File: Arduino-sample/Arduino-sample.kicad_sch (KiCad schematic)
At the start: 7 parts, among them U1 NJM78L05SU3

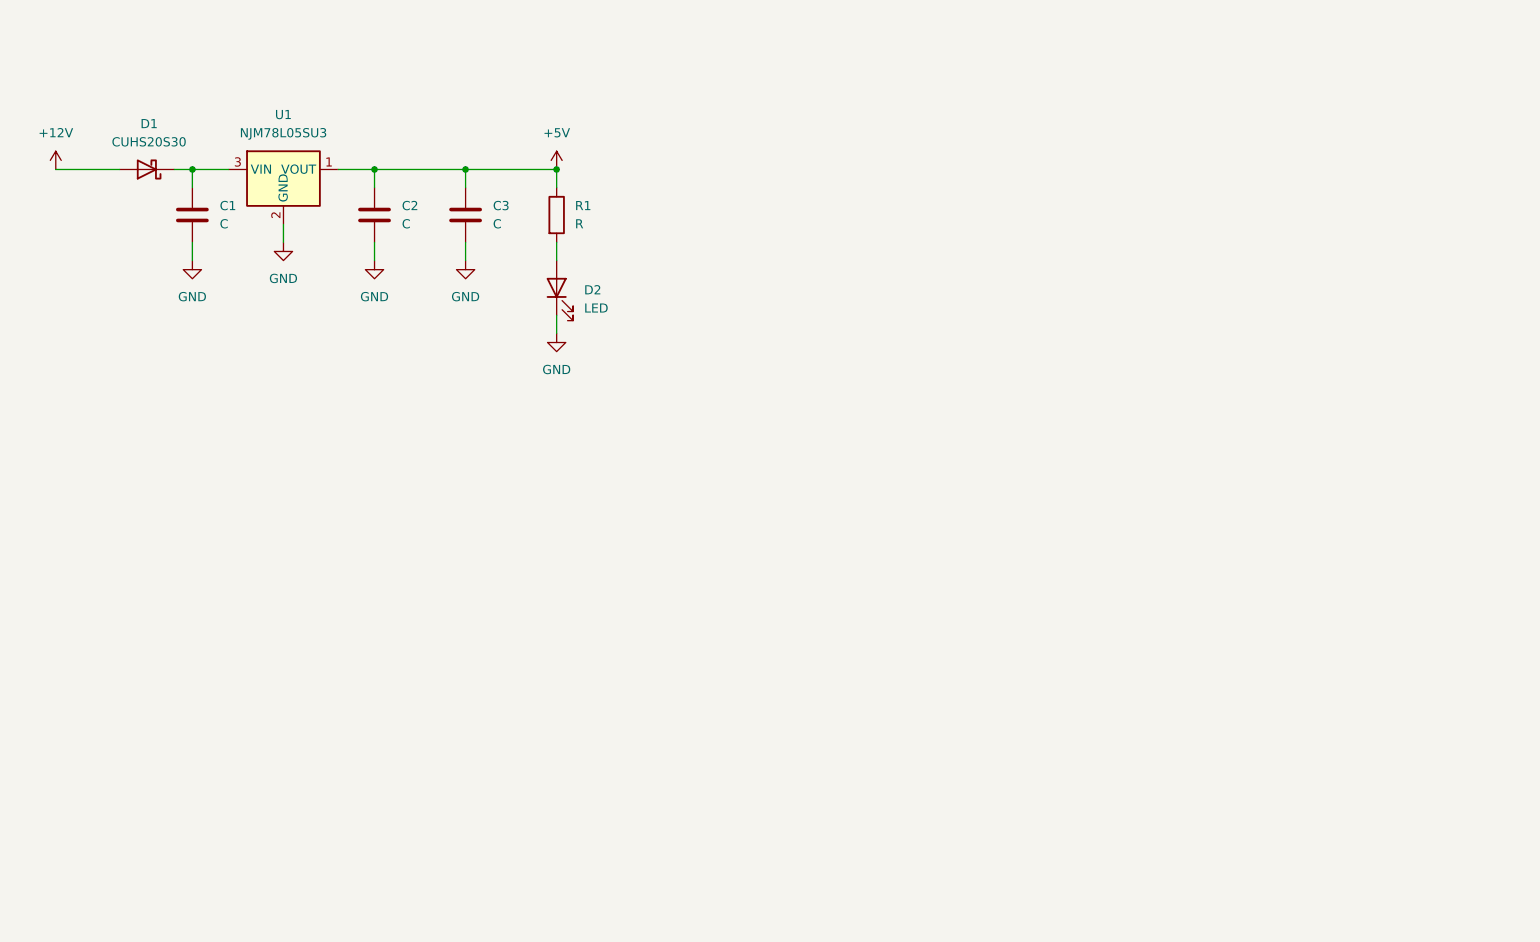
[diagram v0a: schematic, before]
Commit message: マイコン周辺回路追加
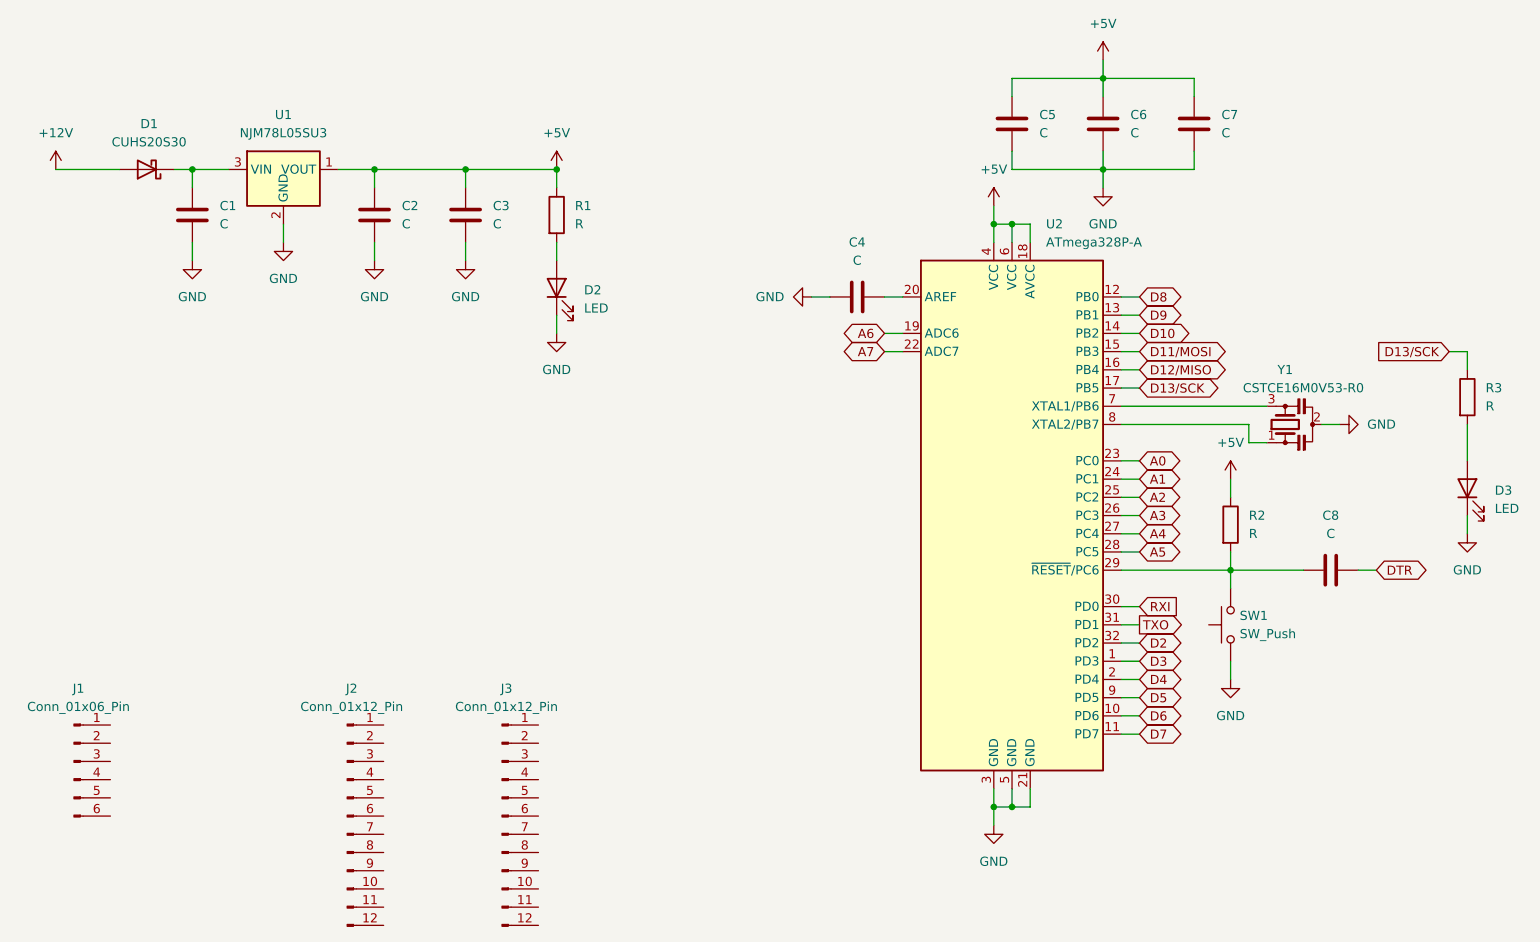
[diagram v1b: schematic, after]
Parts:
- added C4, C5, C6, C7, C8: C, symbol Device:C
- added D3: LED, symbol Device:LED
- added J1: Conn_01x06_Pin, symbol Connector:Conn_01x06_Pin
- added J2, J3: Conn_01x12_Pin, symbol Connector:Conn_01x12_Pin
- added R2, R3: R, symbol Device:R
- added SW1: SW_Push, symbol Switch:SW_Push
- added U2: ATmega328P-A, ProjectEV:TQFP-32_7x7mm_P0.8mm, symbol ProjectEV:ATmega328P-A
- added Y1: CSTCE16M0V53-R0, ProjectEV:CSTCE16M0V53-R0, symbol ProjectEV:CSTCE16M0V53-R0
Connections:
- net +5V: now also C5.1, C6.1, C7.1, R2.1, U2.18 (AVCC), U2.4 (VCC), U2.6 (VCC)
- net GND: now also C4.1, C5.2, C6.2, C7.2, D3.1 (K), SW1.1, U2.21 (GND), U2.3 (GND), U2.5 (GND), Y1.2
- new net: C8.1, R2.2, SW1.2, U2.29 (~{RESET}/PC6)
- new net: D3.2 (A), R3.2
- new net: U2.8 (XTAL2/PB7), Y1.1
- new net: U2.7 (XTAL1/PB6), Y1.3
- new net: C4.2, U2.20 (AREF)
- new net A0: U2.23 (PC0)
- new net A1: U2.24 (PC1)
- new net A2: U2.25 (PC2)
- new net A3: U2.26 (PC3)
- new net A4: U2.27 (PC4)
- new net A5: U2.28 (PC5)
- new net A6: U2.19 (ADC6)
- new net A7: U2.22 (ADC7)
- new net D10: U2.14 (PB2)
- new net D11/MOSI: U2.15 (PB3)
- new net D12/MISO: U2.16 (PB4)
- new net D13/SCK: R3.1, U2.17 (PB5)
- new net D2: U2.32 (PD2)
- new net D3: U2.1 (PD3)
- new net D4: U2.2 (PD4)
- new net D5: U2.9 (PD5)
- new net D6: U2.10 (PD6)
- new net D7: U2.11 (PD7)
- new net D8: U2.12 (PB0)
- new net D9: U2.13 (PB1)
- new net DTR: C8.2
- new net RXI: U2.30 (PD0)
- new net TXO: U2.31 (PD1)
